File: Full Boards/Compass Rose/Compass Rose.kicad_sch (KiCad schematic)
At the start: 245 parts, among them J1 Program Header, J2 Opional Bond, Q10 Onsemi 2N3904TFR, Q11 AO3401A, Q12 Onsemi 2N3904TFR, Q7 AO3401A, Q8 Onsemi 2N3904TFR, Q9 AO3401A, SW1 Boot, SW2 Reset, U2 LM1117MP-5.0, U5 IS31FL3731-SA, U6 FM24CL64B-G, U7 FM24CL64B-G

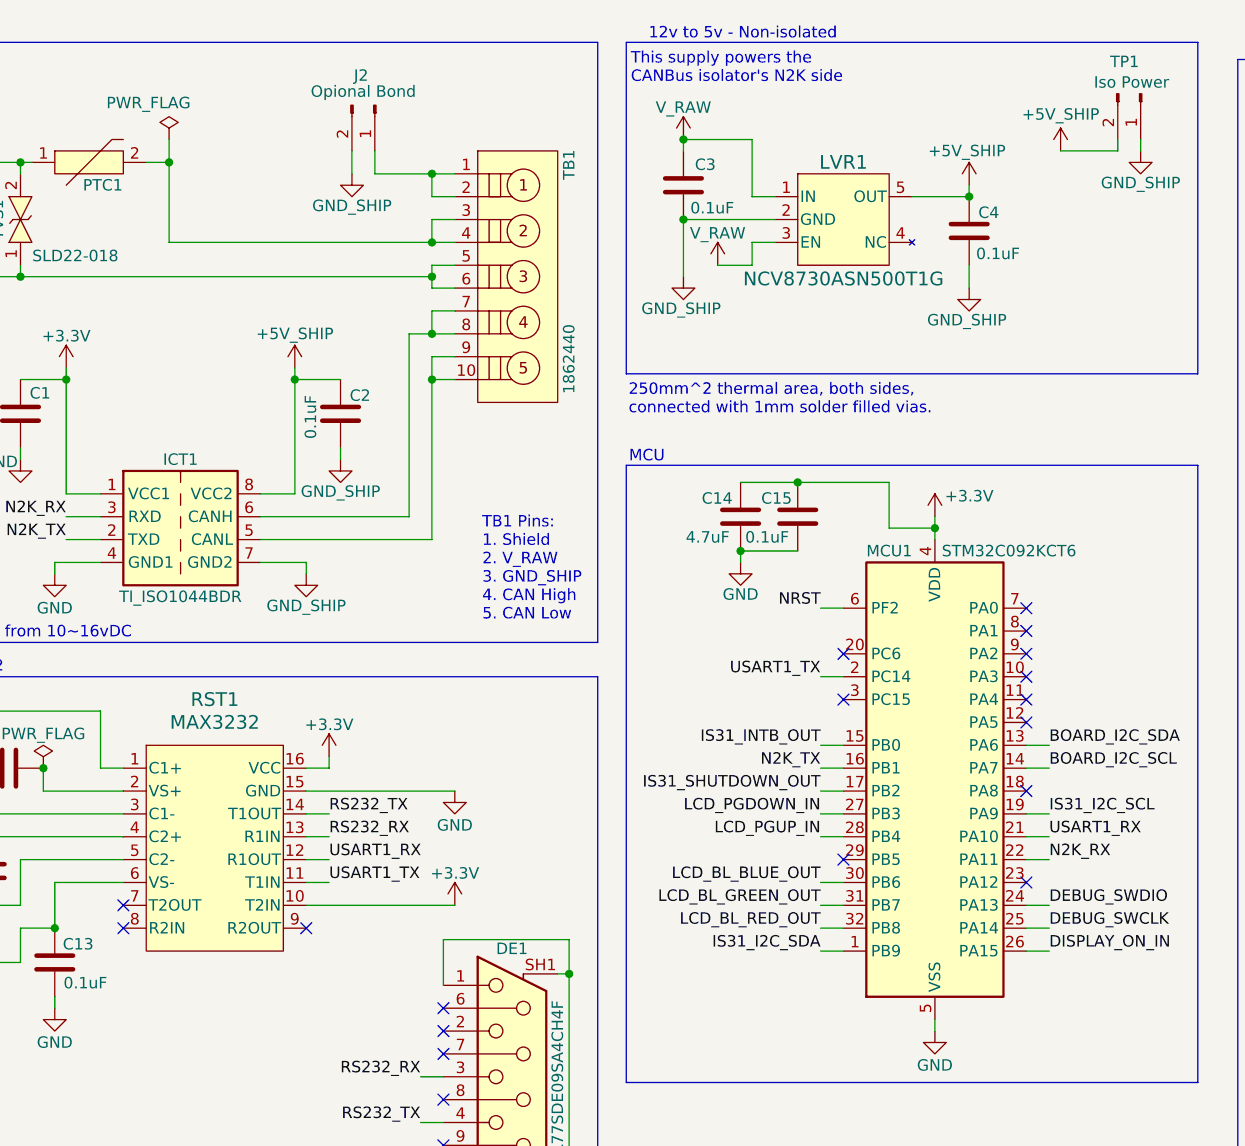
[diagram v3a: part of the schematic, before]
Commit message: Fixed pin types
Signed-off-by: digimer <digital.mermaid@gmail.com>
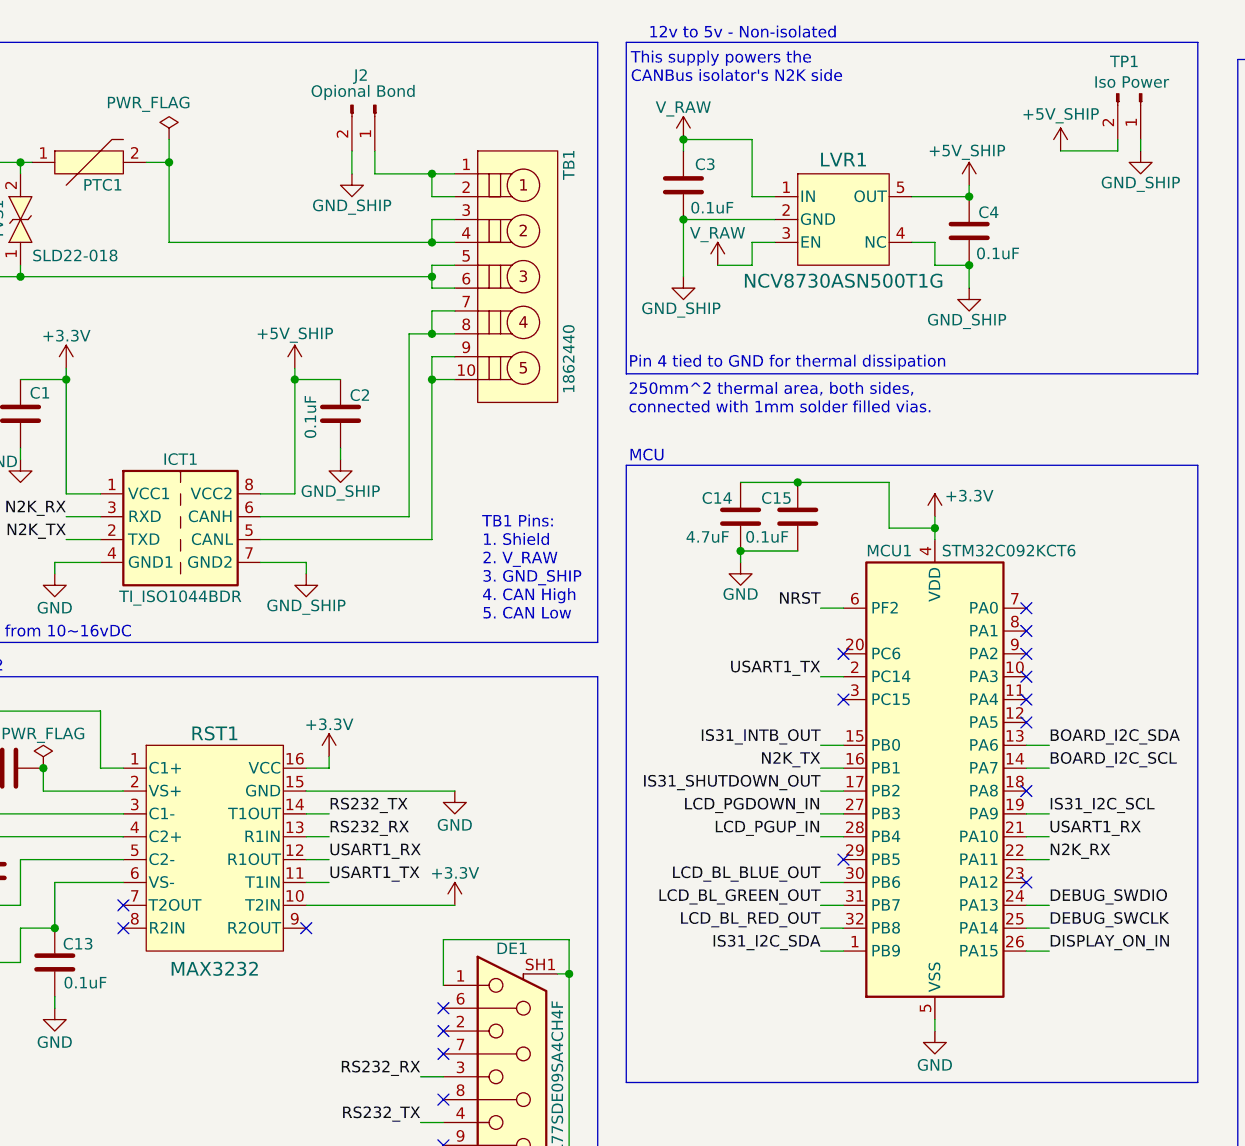
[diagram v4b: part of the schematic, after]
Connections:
- net GND_SHIP: now also LVR1.4 (NC)
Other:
- note added: "Pin 4 tied to GND for thermal dissipation"
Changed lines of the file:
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@@
 		)
 	)
+	(text "Pin 4 tied to GND for thermal dissipation"
+		(exclude_from_sim no)
+		(at 101.854 51.562 0)
+		(effects
+			(font
+				(size 1.27 1.27)
+			)
+			(justify left)
+		)
+	)
 	(text "12v to 5v - Isolated"
 		(exclude_from_sim no)
@@
 	)
 	(junction
+		(at 139.7 40.64)
+		(diameter 0)
+		(color 0 0 0 0)
+	)
+	(junction
 		(at 217.17 290.83)
 		(diameter 0)
@@
 	(wire
 		(pts
+			(xy 135.89 38.1) (xy 135.89 40.64)
+		)
+		(stroke
+			(width 0)
+			(type default)
+		)
+	)
+	(wire
+		(pts
 			(xy 227.33 64.77) (xy 227.33 69.85)
 		)
@@
 	(wire
 		(pts
+			(xy 135.89 40.64) (xy 139.7 40.64)
+		)
+		(stroke
+			(width 0)
+			(type default)
+		)
+	)
+	(wire
+		(pts
 			(xy 64.77 53.34) (xy 69.85 53.34)
 		)
@@
 	(wire
 		(pts
+			(xy 133.35 38.1) (xy 135.89 38.1)
+		)
+		(stroke
+			(width 0)
+			(type default)
+		)
+	)
+	(wire
+		(pts
 			(xy 39.37 294.64) (xy 39.37 297.18)
 		)
@@
 		(in_pos_files yes)
 		(dnp no)
-		(fields_autoplaced yes)
 		(property "Reference" "RST1"
-			(at 55.88 88.9 0)
+			(at 55.88 92.71 0)
 			(show_name no)
 			(do_not_autoplace no)
@@
 		)
 		(property "Value" "MAX3232"
-			(at 55.88 91.44 0)
+			(at 55.88 118.872 0)
 			(show_name no)
 			(do_not_autoplace no)
@@
 		(dnp no)
 		(property "Reference" "LVR1"
-			(at 125.73 29.21 0)
+			(at 125.73 28.956 0)
 			(show_name no)
 			(do_not_autoplace no)
@@
 		)
 		(property "Value" "NCV8730ASN500T1G"
-			(at 125.73 42.164 0)
+			(at 125.73 42.418 0)
 			(show_name no)
 			(do_not_autoplace no)

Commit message: First rework of the Compass Rose schematic.
Signed-off-by: digimer <digital.mermaid@gmail.com>
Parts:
- removed C16, C17, C18: 100uF, Capacitor_THT:CP_Radial_D8.0mm_P5.00mm, symbol Device:C_Polarized
- removed C19: 1uF, Capacitor_THT:C_Rect_L7.2mm_W7.2mm_P5.00mm_FKS2_FKP2_MKS2_MKP2, symbol Device:C
- removed C20, C21: 0.1uF, mr-stuff:RCE5C1H104J2A2H03B, symbol Device:C
- removed C8, C9: 10uF, Capacitor_THT:CP_Radial_D8.0mm_P3.50mm, symbol Device:C_Polarized
- removed D1: 1N5822, Diode_THT:D_DO-201AD_P15.24mm_Horizontal, symbol Diode:1N5822
- removed J2: Opional Bond, Connector_PinHeader_2.54mm:PinHeader_1x02_P2.54mm_Vertical, symbol Connector:Conn_01x02_Pin
- removed LCD1: 2x16 Char RGB I2C, mr-stuff:Newhaven Display NHD-0216K3Z-NS(RGB)-FBW-V3, symbol mr-parts:Newhaven Display NHD-0216K3Z-FS(RGB)-FBW-V3
- removed LVR1: NCV8730ASN500T1G, mr-stuff:Onsemi NCV8730, symbol mr-parts:Onsemi NCV8730ASN500T1G
- removed Q10, Q12, Q8: Onsemi 2N3904TFR, mr-stuff:Onsemi 2N3904TFR, symbol mr-parts:Onsemi 2N3904TFR
- removed Q11, Q7, Q9: AO3401A, Package_TO_SOT_SMD:SOT-23, symbol Transistor_FET:AO3401A
- removed R68: 475, Resistor_THT:R_Axial_DIN0207_L6.3mm_D2.5mm_P7.62mm_Horizontal, symbol Device:R
- removed TP10, TP12: +5V_SHIP, Connector_PinHeader_2.54mm:PinHeader_1x01_P2.54mm_Vertical, symbol Connector:Conn_01x01_Pin
- removed TP11, TP13: GND_SHIP, Connector_PinHeader_2.54mm:PinHeader_1x01_P2.54mm_Vertical, symbol Connector:Conn_01x01_Pin
- removed TP3: N2K_RX, Connector_PinHeader_2.54mm:PinHeader_1x01_P2.54mm_Vertical, symbol Connector:Conn_01x01_Pin
- removed TP4: N2K_TX, Connector_PinHeader_2.54mm:PinHeader_1x01_P2.54mm_Vertical, symbol Connector:Conn_01x01_Pin
- removed TP7: +5V, Connector_PinHeader_2.54mm:PinHeader_1x01_P2.54mm_Vertical, symbol Connector:Conn_01x01_Pin
- removed TP8: GND, Connector_PinHeader_2.54mm:PinHeader_1x01_P2.54mm_Vertical, symbol Connector:Conn_01x01_Pin
- removed TP9: +3.3V, Connector_PinHeader_2.54mm:PinHeader_1x01_P2.54mm_Vertical, symbol Connector:Conn_01x01_Pin
- removed TVS2, TVS3, TVS4: PESD3V3L1BA, Diode_SMD:D_SOD-323, symbol mr-parts:UMW_PESD3V3L1BA
- removed U2: LM1117MP-5.0, Package_TO_SOT_SMD:SOT-223-3_TabPin2, symbol Regulator_Linear:LM1117MP-5.0
- removed U5: IS31FL3731-SA, Package_SO:SSOP-28_5.3x10.2mm_P0.65mm, symbol Driver_LED:IS31FL3731-SA
- removed U6, U7: FM24CL64B-G, Package_SO:SOIC-8_3.9x4.9mm_P1.27mm, symbol Memory_NVRAM:FM24C64B
- added C16, C29, C30, C31, C9: 0.1uF, mr-stuff:Kyocera AVX 0805, symbol Device:C
- added C17, C18: 16pF, mr-stuff:Kemet C0603X, symbol Device:C
- added C19, C20, C21: 100uF, Capacitor_THT:CP_Radial_D8.0mm_P5.00mm, symbol Device:C_Polarized
- added C28: 100pF, mr-stuff:Kemet C0805X, symbol Device:C
- added C8: 22uF, mr-stuff:Murata GCJ31CR71A, symbol Device:C
- added CMC1: ACT12101012PTL00, mr-stuff:TDK ACT12101012PTL00, symbol mr-parts:TDK ACT1210-510-2P-TL00
- added CPD1: IS31FL3731-SA, Package_SO:SSOP-28_5.3x10.2mm_P0.65mm, symbol mr-parts:Lumissil IS31FL3731-SALS2-TR
- added J3: Optional Bond, Connector_PinHeader_2.54mm:PinHeader_1x02_P2.54mm_Vertical, symbol Connector:Conn_01x02_Pin
- added LCD2: NHD-0216K3Z-NS(RGB)-FBW-V3, mr-stuff:Newhaven Display NHD-0216K3Z-NS(RGB)-FBW-V3, symbol mr-parts:Newhaven Display NHD-0216K3Z-FS(RGB)-FBW-V3
- added LS1: TI PCA9306IDCURQ1, mr-stuff:TI PCA9306, symbol mr-parts:TI PCA9306IDCURQ1
- added LVR1: BD450S5FP-CE2, mr-stuff:Rohm BD4xxS5-C, symbol mr-parts:Rohm BD450S5FP-CE2
- added LVR2: BD33C0AFP-CE2, mr-stuff:Rohm BD33C0, symbol mr-parts:BD33C0AFP-CE2
- added OX1: 12.60378, Crystal:Crystal_SMD_3225-4Pin_3.2x2.5mm, symbol mr-parts:Geyer 12.60378
- added Q1, Q3, Q5: BSS314PE, Package_TO_SOT_SMD:SOT-23, symbol mr-parts:Infineon BSS314PE
- added Q2, Q4, Q6: DMN6075S, Package_TO_SOT_SMD:SOT-23, symbol Transistor_FET:DMN6075S
- added R27: 475, Resistor_THT:R_Axial_DIN0207_L6.3mm_D2.5mm_P7.62mm_Horizontal, symbol Device:R
- added R28: 10k, Resistor_THT:R_Axial_DIN0207_L6.3mm_D2.5mm_P7.62mm_Horizontal, symbol Device:R
- added ROM1, ROM2: M24C64, mr-stuff:STM M24C64-RMN6P, symbol mr-parts:STM_M24C64-RMN6P
- added SD1: 1N5822RL, mr-stuff:STM 1N5822RL, symbol Device:D_Schottky
- added TP1: Ship Power, Connector_PinHeader_2.54mm:PinHeader_1x05_P2.54mm_Vertical, symbol Connector:Conn_01x05_Pin
- added TP10: IS31 I2C, Connector_PinHeader_2.54mm:PinHeader_1x01_P2.54mm_Vertical, symbol Connector:Conn_01x02_Pin
- added TP11: Board I2C, Connector_PinHeader_2.54mm:PinHeader_1x01_P2.54mm_Vertical, symbol Connector:Conn_01x02_Pin
- added TP3: Board Power, Connector_PinHeader_2.54mm:PinHeader_1x05_P2.54mm_Vertical, symbol Connector:Conn_01x05_Pin
- added TVS2: PESD2CANFD54VT-QR, mr-stuff:Nexperia PESD2CANFD, symbol mr-parts:Nexperia PESD2CANFD54VT-QR
- added TVS3, TVS4: TPD2E2U06QDBZRQ1, mr-stuff:TI TPD2E2U06, symbol mr-parts:TVS TPD2E2U06QDBZRQ1
- C1, C10, C11, C12, C13, C15, C2, C23, C24, C25, C26, C3: footprint mr-stuff:RCE5C1H104J2A2H03B -> mr-stuff:Kyocera AVX 0805; Part (none) -> Kyocera 08051C104K4Z2A
- C14: footprint mr-stuff:Murata RCER71E -> mr-stuff:Kyocera AVX 1206; Part (none) -> Kyocera 12065C475K4Z2A
- C22: value 0.1uF -> 1uF; footprint mr-stuff:RCE5C1H104J2A2H03B -> mr-stuff:Kemet R82DC; Part (none) -> Kemet R82DC4100DQ60J
- C27: value 0.1uF -> 0.01uF; footprint mr-stuff:RCE5C1H104J2A2H03B -> mr-stuff:TDK FA 2.5mm; Part (none) -> TDK FA18NP01H103JNU06
- C4: value 0.1uF -> 22uF; footprint mr-stuff:RCE5C1H104J2A2H03B -> mr-stuff:Murata GCJ31CR71A; Part (none) -> Murata GCJ31CR71A226KE01L
- C5: footprint Capacitor_THT:CP_Radial_D8.0mm_P3.50mm -> mr-stuff:Nichicon UBT; Part (none) -> Nichicon UBT1H100MPD8
- C6: value 1500 pF -> 1nF; footprint mr-stuff:TDK FA 5.0mm -> mr-stuff:Knowles Syfer 2211JA25; Part TDK FA28NP01H152JNU06 -> Knowles Syfer 2211JA250102JKTSYX; now not fitted
- C7: value 0.1uF -> 10uF; footprint mr-stuff:RCE5C1H104J2A2H03B -> mr-stuff:TDK CGA5; Part (none) -> TDK CGA5L1X7R1E106K160DC
- DE2: value (none) -> L777SDE09PA4CH4F; Part (none) -> AAmphenol L777SDE09PA4CH4F
- ICT1: value TI_ISO1044BDR -> ISO1044BD; footprint Package_SO:SOIC-8_3.9x4.9mm_P1.27mm -> mr-stuff:TI ISO1044BDR
- IDCB1: Arrow Part Number SPBW06F-05 -> (none); Arrow Price/Stock https://www.arrow.com/en/products/spbw06f-05/mean-well-ente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 -> (none); Height 11.6 -> (none); Manufacturer_Name Mean Well -> (none); Manufacturer_Part_Number SPBW06F-05 -> (none); Mouser Part Number 709-SPBW06F-05 -> (none); Mouser Price/Stock https://www.mouser.co.uk/ProductDetail/MEAN-WELL/SPBW06F-05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 -> (none)
- L1: Part (none) -> Pulse PA4340.103NLT
- R1: value 4.7K -> 10k; Part (none) -> Stackpole RMCA0805FT10K0-HP
- R10, R13, R7: value 10K -> 10k; Part (none) -> Stackpole RMCA0805FT10K0-HP
- R11, R14: value 63.4 -> 68.1; footprint Resistor_THT:R_Axial_DIN0207_L6.3mm_D2.5mm_P7.62mm_Horizontal -> mr-stuff:Stackpole RNCP0805; Part (none) -> Stackpole RNCP0805FTD68R1
- R12, R15, R9: value 1K -> 1k; footprint Resistor_THT:R_Axial_DIN0207_L6.3mm_D2.5mm_P7.62mm_Horizontal -> mr-stuff:Stackpole RNCP0805; Part (none) -> Stackpole RNCP0805FTD1K00
- R16: value 10K -> 200K; Part (none) -> KOA Speer MF1/4CCT52R2003F
- R17, R18: value 10K -> 4.7k; footprint Resistor_THT:R_Axial_DIN0207_L6.3mm_D2.5mm_P7.62mm_Horizontal -> mr-stuff:Stackpole RMCA0805; Part (none) -> Stackpole RMCA0805FT4K70-HP
- R19, R20: value 10K -> 3.3k; footprint Resistor_THT:R_Axial_DIN0207_L6.3mm_D2.5mm_P7.62mm_Horizontal -> mr-stuff:Stackpole RNCF0805; Part (none) -> Stackpole RNCF0805DTE3K30
- R2: value 4.7K -> 10k; Part (none) -> Stackpole RMCA0805FT10K0-HP; now not fitted
- R21, R22: value 475 -> 10k; Part (none) -> Stackpole RMCA0805FT10K0-HP
- R23, R25: value 3.3K -> 475
- R24, R26: value 3.3K -> 10k; Part (none) -> Stackpole RMCA0805FT10K0-HP
- R3: value 4.7K -> 4.7k; footprint Resistor_THT:R_Axial_DIN0207_L6.3mm_D2.5mm_P7.62mm_Horizontal -> mr-stuff:Stackpole RMCA0805; Part (none) -> Stackpole RMCA0805FT4K70-HP
- R4: value 100K -> 20k; footprint Resistor_THT:R_Axial_DIN0207_L6.3mm_D2.5mm_P7.62mm_Horizontal -> mr-stuff:Stackpole RMCA0805; Part (none) -> Stackpole RMCA0805FT20K0-HP
- R5: value 4.7K -> 3.3k; footprint Resistor_THT:R_Axial_DIN0207_L6.3mm_D2.5mm_P7.62mm_Horizontal -> mr-stuff:Stackpole RNCF0805; Part (none) -> Stackpole RNCF0805DTE3K30
- R6: value 3.3K -> 3.3k; footprint Resistor_THT:R_Axial_DIN0207_L6.3mm_D2.5mm_P7.62mm_Horizontal -> mr-stuff:Stackpole RNCF0805; Part (none) -> Stackpole RNCF0805DTE3K30
- R8: footprint Resistor_THT:R_Axial_DIN0207_L6.3mm_D2.5mm_P7.62mm_Horizontal -> mr-stuff:Stackpole RNCP0805; Part (none) -> Stackpole RNCP0805FTD150R
- TVS1: Part Littelfuse SLD22-018 -> LittelFuse SLD22-018
- renumbered TP1 to TP2
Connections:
- net +3.3V: now also C1.2, C10.2, C13.2, C15.2, C25.2, C26.2, R1.1, R21.2, R24.2, R5.2, R6.2, C8.2, LS1.2 (VREF1), LVR2.3 (Vout), R28.2, ROM1.1 (E0), ROM1.3 (E2), ROM1.8 (VCC), ROM2.1 (E0), ROM2.2 (E1), ROM2.3 (E2), ROM2.8 (VCC), TP3.1 (Pin_1); no longer C1.1, C12.1, C15.1, C23.1, C24.1, DE2.2, R16.1, R18.2, R23.1, R24.1, R25.1
- net +5V: now also C22.1, C23.2, C7.2, R10.2, R13.2, R16.2, R17.1, R18.2, R7.2, C19.1, C20.1, C21.1, CPD1.2 (VCC), CPD1.3 (~{SDB}), LCD2.3 (+5V), LCD2.9 (+5V), LVR2.1 (Vcc), Q1.2 (S), Q3.2 (S), Q5.2 (S), TP3.5 (Pin_5); no longer C6.2, R1.1, R10.1, R13.1, R7.1
- net +5V_SHIP: now also C2.2, C4.2, LVR1.3 (VOUT), TP1.1 (Pin_1); no longer C2.1, C4.1
- net BOARD_I2C_SCL: now also R6.1, CPD1.20 (SCL), LS1.3 (SCL1), ROM1.6 (SCL), ROM2.6 (SCL), TP11.2 (Pin_2); no longer R25.2
- net BOARD_I2C_SDA: now also R5.1, CPD1.19 (SDA), LS1.4 (SDA1), ROM1.5 (SDA), ROM2.5 (SDA), TP11.1 (Pin_1); no longer R26.2
- net CA1: now also CPD1.21 (CA1)
- net CA2: now also CPD1.22 (CA2)
- net CA3: now also CPD1.23 (CA3)
- net CA4: now also CPD1.24 (CA4)
- net CA5: now also CPD1.25 (CA5)
- net CA6: now also CPD1.26 (CA6)
- net CA7: now also CPD1.27 (CA7)
- net CA8: now also CPD1.28 (CA8)
- net CA9: now also CPD1.1 (CA9)
- net CB1: now also CPD1.7 (CB1)
- net CB2: now also CPD1.8 (CB2)
- net CB3: now also CPD1.9 (CB3)
- net CB4: now also CPD1.10 (CB4)
- net CB5: now also CPD1.11 (CB5)
- net CB6: now also CPD1.12 (CB6)
- net CB7: now also CPD1.13 (CB7)
- net CB8: now also CPD1.14 (CB8)
- net CB9: now also CPD1.15 (CB9)
- net DEBUG_SWCLK: now also R22.2; no longer R17.1
- net DISPLAY_ON_IN: now also C31.2, R27.2, R28.1; no longer C27.1, R20.1, R22.2
- net DISPLAY_ON_IN_PLUG: now also R27.1, TVS4.1 (IO1); no longer R22.1
- net GND: now also C1.1, C12.1, C15.1, C23.1, C24.1, C25.1, C26.1, C6.2, C7.1, DE1.5, DE2.7, R22.1, R4.1, C16.1, C17.2, C18.1, C19.2, C20.2, C21.2, C28.1, C29.1, C30.2, C31.1, C8.1, CPD1.17 (IN), CPD1.18 (AD), CPD1.5 (GND), LCD2.10 (GND), LCD2.2 (GND), LCD2.8 (GND), LS1.1 (GND), LVR2.2 (Gnd), OX1.2, OX1.4, Q2.2 (S), Q4.2 (S), Q6.2 (S), ROM1.2 (E1), ROM1.4 (VSS), ROM1.7 (~{WC}), ROM2.4 (VSS), ROM2.7 (~{WC}), TP3.3 (Pin_3), TVS3.3 (GND), TVS4.3 (GND); no longer C1.2, C15.2, C23.2, C24.2, C25.2, C26.2, C7.2, DE1.1, R17.2, R4.2, R5.2, R6.2
- net GND_SHIP: now also C2.1, C3.1, C4.1, C6.1, TVS1.2, J3.2 (Pin_2), LVR1.4 (GND), TP1.3 (Pin_3), TVS2.3; no longer C2.2, C3.2, C4.2, C7.1, TVS1.1
- net IS31_I2C_SCL: now also R20.1, TP10.2 (Pin_2); no longer R2.2, R23.2
- net IS31_I2C_SDA: now also R19.1, TP10.1 (Pin_1); no longer R24.2, R3.2
- net IS31_INTB_OUT: now also R3.2, CPD1.4 (~{INTB}); no longer R1.2
- net LCD_BL_BLUE_OUT: now also R15.1; no longer R15.2
- net LCD_BL_GREEN_OUT: now also R12.1; no longer R12.2
- net LCD_BL_RED_OUT: now also R9.1; no longer R9.2
- net LCD_PGDOWN_IN: now also R25.2, R26.2, C30.1; no longer C26.1, R19.1, R21.2
- net LCD_PGDOWN_IN_PLUG: now also R25.1, TVS3.2 (IO2); no longer R21.1
- net LCD_PGUP_IN: now also R23.2, R24.1, C29.2; no longer C25.1, R18.1
- net LCD_PGUP_IN_PLUG: now also R23.1, TVS3.1 (IO1)
- net NRST: now also R21.1, C16.2; no longer C22.1, R16.2
- net RS232_RX: now also DE1.2; no longer DE1.3
- net RS232_TX: now also DE1.3; no longer DE1.4
- net USART1_RX: now also MCU1.8 (PA1); no longer MCU1.21 (PA10)
- net USART1_TX: now also MCU1.7 (PA0); no longer MCU1.2 (PC14)
- net V_RAW: now also C3.2, LVR1.1 (VCC), SD1.1 (K), TP1.5 (Pin_5); no longer C3.1
- net at RST1.1 (C1+): now also C9.2; no longer C10.1
- net at RST1.2 (VS+): now also C10.1; no longer C12.2
- net at RST1.3 (C1-): now also C9.1; no longer C10.2
- net at RST1.4 (C2+): now also C11.2; no longer C11.1
- net at RST1.5 (C2-): now also C11.1; no longer C11.2
- net at RST1.6 (VS-): now also C12.2; no longer C13.2
- net at R11.1: now also Q3.3 (D)
- net at IDCB1.2 (+VIN), L1.2: no longer C6.1
- net at PTC1.1: now also TVS1.1, SD1.2 (A); no longer TVS1.2
- net at TB1.1, TB1.2: now also J3.1 (Pin_1)
- net N2K_CAN_L: now reaches TB1.10, TB1.9
- net N2K_CAN_L: now also CMC1.3 (O2), TVS2.2; no longer ICT1.5 (CANL)
- net N2K_CAN_H: now reaches TB1.7, TB1.8
- net N2K_CAN_H: now also CMC1.4 (O1), TVS2.1; no longer ICT1.6 (CANH)
- net at MCU1.10 (PA3): now also R2.2
- net OSC_OUT: now reaches MCU1.3 (PC15)
- net OSC_OUT: now also C18.2, OX1.3
- net at MCU1.9 (PA2): now also R1.2
- net at R11.2: now also LCD2.12 (A-GREEN)
- net at R14.1: now also Q5.3 (D)
- net at R14.2: now also LCD2.13 (A-BLUE)
- net at R8.1: now also Q1.3 (D)
- net at R8.2: now also LCD2.11 (A-RED)
- net IS31_SHUTDOWN_OUT: no longer names the net of MCU1.17 (PB2)
- net IS31_SHUTDOWN_OUT: no longer R4.1
- net N2K_RX renamed N2K_FDCAN_RX
- net N2K_TX renamed N2K_FDCAN_TX
- new net: LCD2.7 (SDA), LS1.5 (SDA2), R18.1
- new net: LCD2.6 (SCL), LS1.6 (SCL2), R17.2
- new net: C27.1, C28.2, LS1.7 (VREF2), LS1.8 (EN), R16.1
- new net: Q5.1 (G), Q6.3 (D), R13.1
- new net: Q2.1 (G), R9.2
- new net: Q1.1 (G), Q2.3 (D), R7.1
- new net: CMC1.1 (I1), ICT1.6 (CANH)
- new net: CMC1.2 (I2), ICT1.5 (CANL)
- new net: Q3.1 (G), Q4.3 (D), R10.1
- new net: Q6.1 (G), R15.2
- new net: Q4.1 (G), R12.2
- new net: C24.2, CPD1.16 (C_FILT)
- new net: CPD1.6 (R_EXT), R4.2
- new net OSC_IN: C17.1, MCU1.2 (PC14), OX1.1
- no-connect marks 27 -> 28
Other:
- note added: "-=] Config PA2 | PA3 | Task ---+---+---------- 0 | 0 | Undefined 0 | 1 | Heading Mode 1 | 0 | Wind Instrument 1 | 1 | Future Use ---+---+----------"
- note added: "-=] DE2 1 - nc 2 - nc 3 - Display On Switch 4 - LCD Page Down Switch 5 - LCD Page Up Switch 6 - nc 7 - ESD Ground 8 - Ground (Display On) 9 - Ground (LCD Paging)"
- note added: "C4 provided for optional Common Mode EMI suppression"
- note added: "Charliplex LED Driver"
- note added: "High-Speed External Crystal"
- note added: "I2C Addr: 0x28"
- note added: "I2C Addr: 0x74"
- note added: "Isolated 5v to 3.3v"
- note added: "NOTE: IS31FL373Ω is powered from the +5V rail to allow for higher voltage LEDs. The I2C bus operates natively at 3.3V. This logic mismatch is validated. The minimum High-Level Input Voltage V{IH} of 1.4V. The 3.3V logic exceeds this threshold. A level shifter is intentionally omitted."
- note added: "Place as close to MCU pins as possible. Add ground ring with vias as Faraday cage."
- note added: "Use conductive tape on the back-side of the plexi and tie it to pin 7."
- note added: "V_RAW can be 10~16 VDC TB1 connect to Amphenol MSAS-05PMMC-SF8C15"
- note removed: "*V_RAW can vary from 10~16vDC"
- note removed: "-=] DE2 1 - nc 2 - nc 3 - Display On Switch 4 - LCD Page Down Switch 5 - LCD Page Up Switch 6 - Brightness Pot 7 - nc 8 - Ground (Display On) 9 - Ground (LCD Paging)"
- note removed: "5v to 3.3v"
- note removed: "LED Driver"
- note removed: "Put close to MCU!"
- moved on the sheet: C14, DE1, DE2, FID1, FID2, FID3, H1, H2, H3, H4, J1, LED1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

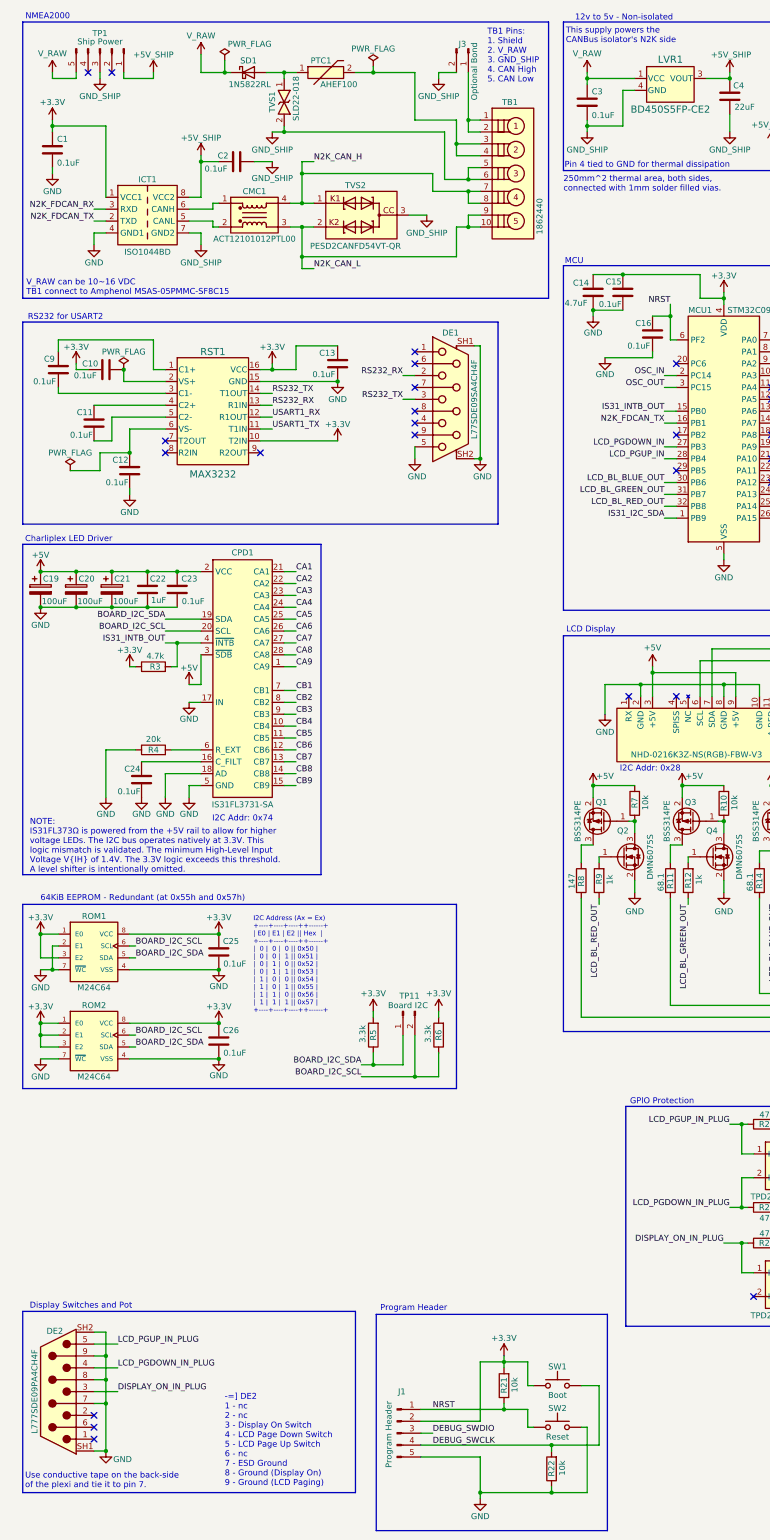
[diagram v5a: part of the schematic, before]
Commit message: Fixed wrong pin type for the BD450S5FP-CE2. Fixed IS31 I2C bus. Fixed RS-232 DE1 pinout. Fixed test point footprints.
Signed-off-by: digimer <digital.mermaid@gmail.com>
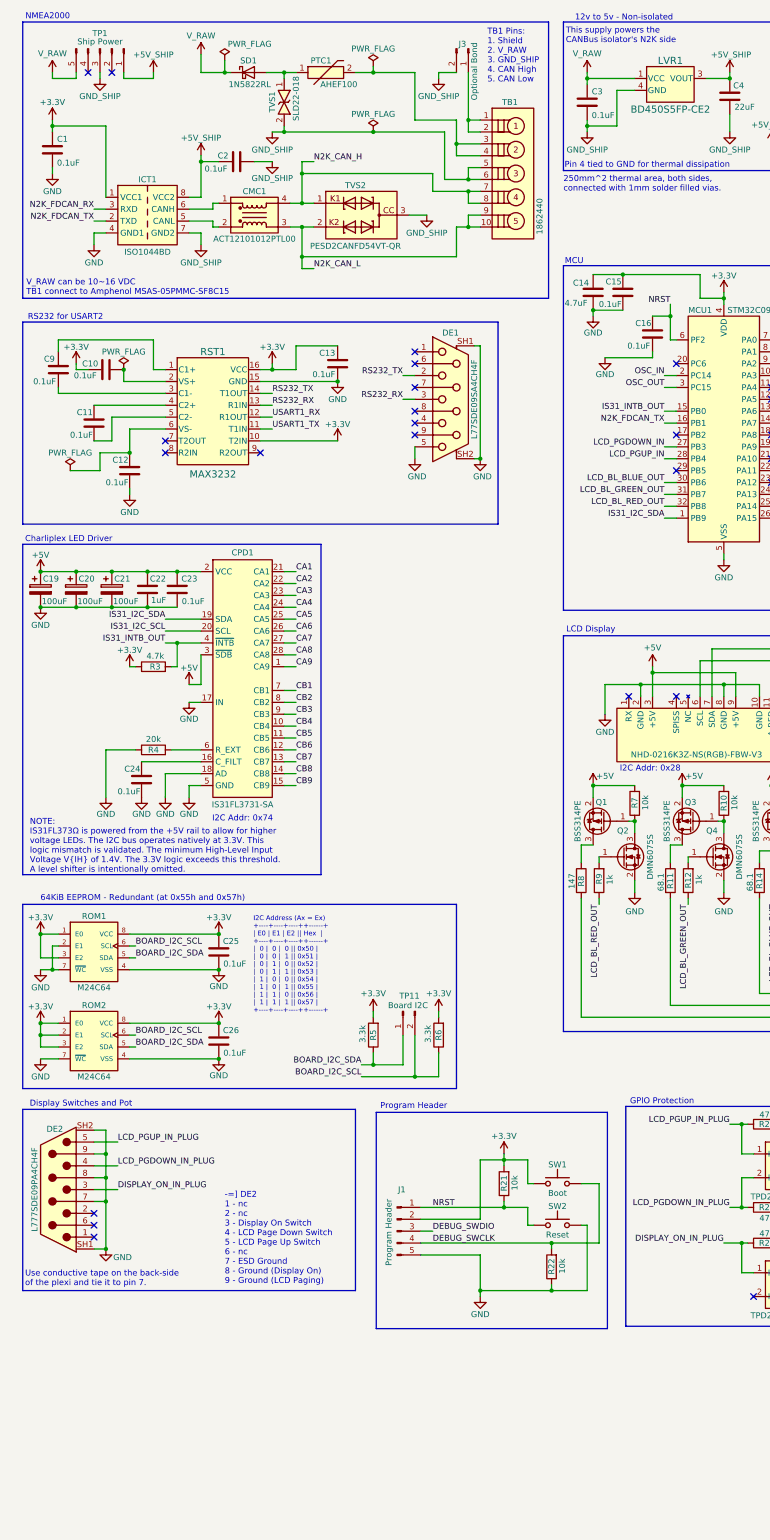
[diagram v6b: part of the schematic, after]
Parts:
- TP10, TP11, TP2: footprint Connector_PinHeader_2.54mm:PinHeader_1x01_P2.54mm_Vertical -> Connector_PinHeader_2.54mm:PinHeader_1x02_P2.54mm_Vertical
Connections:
- net BOARD_I2C_SCL: no longer CPD1.20 (SCL)
- net BOARD_I2C_SDA: no longer CPD1.19 (SDA)
- net IS31_I2C_SCL: now also CPD1.20 (SCL)
- net IS31_I2C_SDA: now also CPD1.19 (SDA)
- net RS232_RX: now also DE1.3; no longer DE1.2
- net RS232_TX: now also DE1.2; no longer DE1.3
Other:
- moved on the sheet: DE2, J1, R21, R22, SW1, SW2
